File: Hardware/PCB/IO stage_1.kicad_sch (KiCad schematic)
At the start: 56 parts, among them IC10 THS4281DBVT, IC11 M74VHC1GT126DT1G, IC13 M74VHC1GT126DT1G, IC14 M74VHC1GT126DT1G, IC15 M74VHC1GT126DT1G, IC16 M74VHC1GT126DT1G, IC17 M74VHC1GT126DT1G, IC18 M74VHC1GT126DT1G, IC19 M74VHC1GT126DT1G, IC2 M74VHC1GT126DT1G, IC20 M74VHC1GT126DT1G, IC21 M74VHC1GT126DT1G, IC22 M74VHC1GT126DT1G, IC4 M74VHC1GT126DT1G, IC5 M74VHC1GT126DT1G, IC6 M74VHC1GT126DT1G, X1 conn 1x5 2, X10 conn 1x3, X2 conn 1x5, X3 conn 1x2, X4 conn 1x3, X5 conn 1x5, X9 conn 1x5

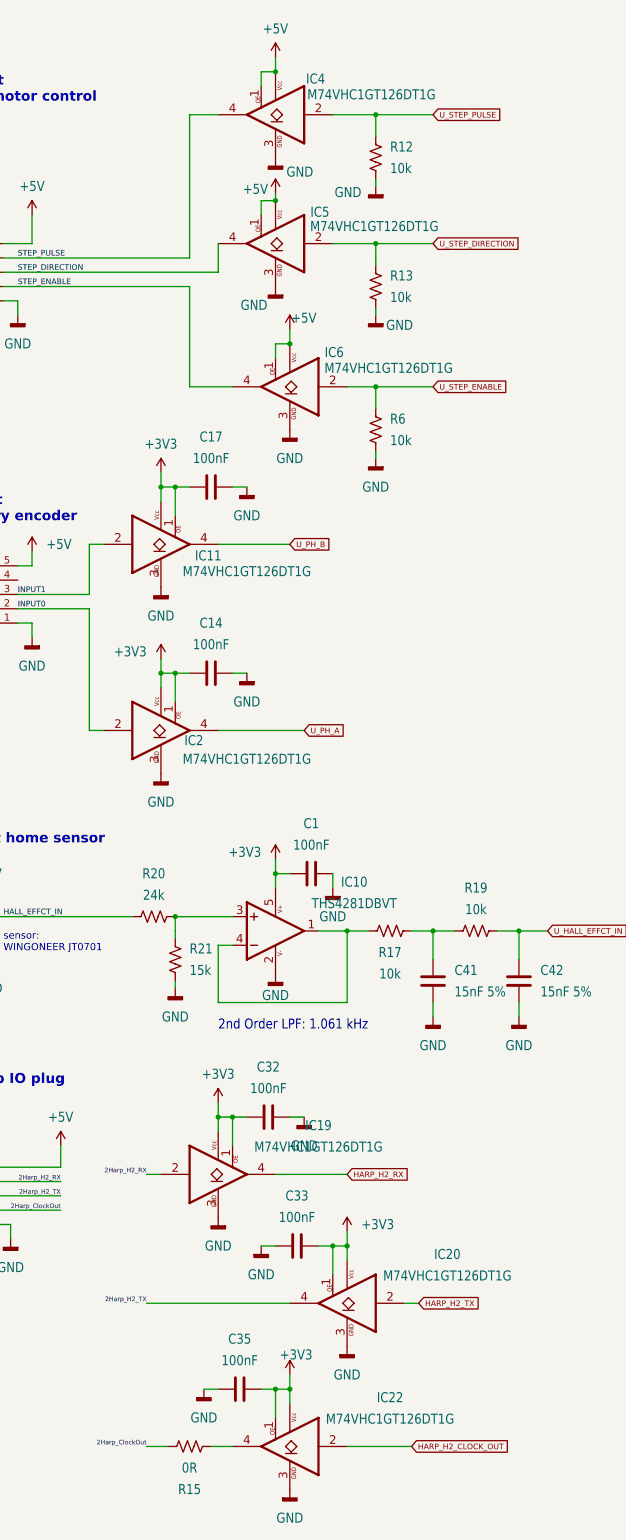
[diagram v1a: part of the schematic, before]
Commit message: DRC=0; mudanças faladas com Neurogears @12Junho OK
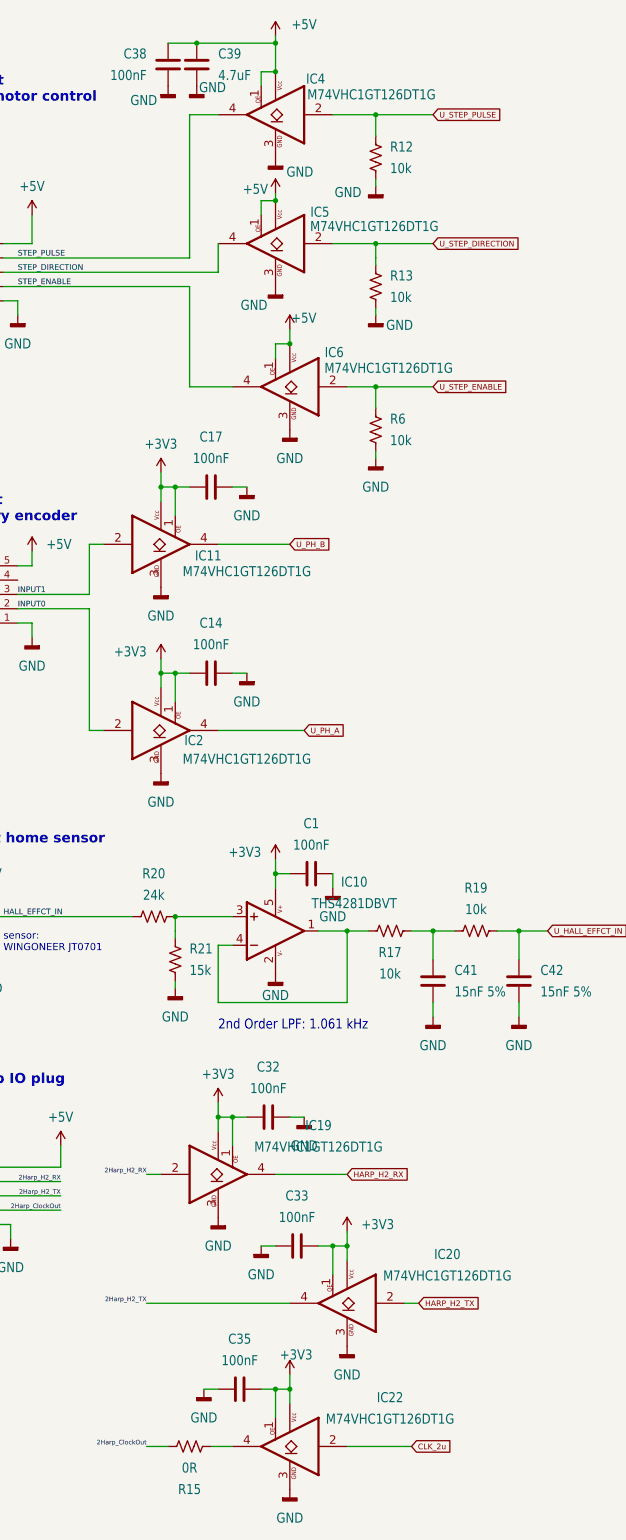
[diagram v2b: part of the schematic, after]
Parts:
- added C38: 100nF, Capacitor_SMD:C_0402_1005Metric, symbol Device:C
- added C39: 4.7uF, Capacitor_SMD:C_0603_1608Metric, symbol Device:C
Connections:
- net +5V: now also C38.2, C39.1
- net GND: now also C38.1, C39.2
- net HARP_H2_CLOCK_OUT renamed CLK_2u

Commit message: MPN & OEPSPN adicionados; ainda em falta novos PNs a ser emitidos
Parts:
- C1, C14, C17, C19, C20, C21, C22, C30, C31, C32, C33, C34, C35, C38: MPN C1005X7R1H104K050BB -> CGA2B3X7R1H104K050BB; OEPS OEPS010004 -> (none); OEPSPN (none) -> OEPS010016
- C39: OEPS OEPS010018 -> (none); OEPSPN (none) -> OEPS010018
- C41, C42: MPN CGA2B3X7R1V153K050BB -> TBD 15nF 5%; OEPS OEPS010023 -> (none)
- IC10: OEPS OEPS080038 -> (none); OEPSPN (none) -> OEPS080038
- IC11, IC13, IC14, IC15, IC16, IC17, IC18, IC19, IC2, IC20, IC21, IC22, IC4, IC5, IC6: DIGIKEY_PN M74VHC1GT126DT1GOSDKR-ND -> (none); OEPS OEPS080017 -> (none); OEPSPN (none) -> OEPS080017
- R10, R11, R12, R13, R14, R16, R17, R19, R22, R23, R6, R8: MPN CRCW040210K0FKED -> ERJ-2RKF1002X; OEPS OEPS020030 -> (none); OEPSPN (none) -> OEPS020013
- R15: MPN TBD -> RC0402JR-070RL; OEPS TBD -> (none); OEPSPN (none) -> OEPS020001
- R20: OEPS OEPS020048 -> (none); OEPSPN (none) -> OEPS020048
- R21: OEPS OEPS020015 -> (none); OEPSPN (none) -> OEPS020015
- X1: OEPS OEPS070037 -> (none); OEPSPN (none) -> OEPS070037
- X10, X4: OEPS OEPS070035 -> (none); OEPSPN (none) -> OEPS070035
- X2, X5, X9: OEPS OEPS070041 -> (none); OEPSPN (none) -> OEPS070041
- X3: OEPS OEPS070035 -> (none); OEPSPN (none) -> OEPS070020
